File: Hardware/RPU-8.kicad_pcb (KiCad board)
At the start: 4 copper layers, 139.7 x 55.9 mm, 5 parts, among them J1 ADDR_BUS, J2 DATA_BUS, J3 Conn_01x03_Female, J4 CTRL_BUS, J5 INST_REG

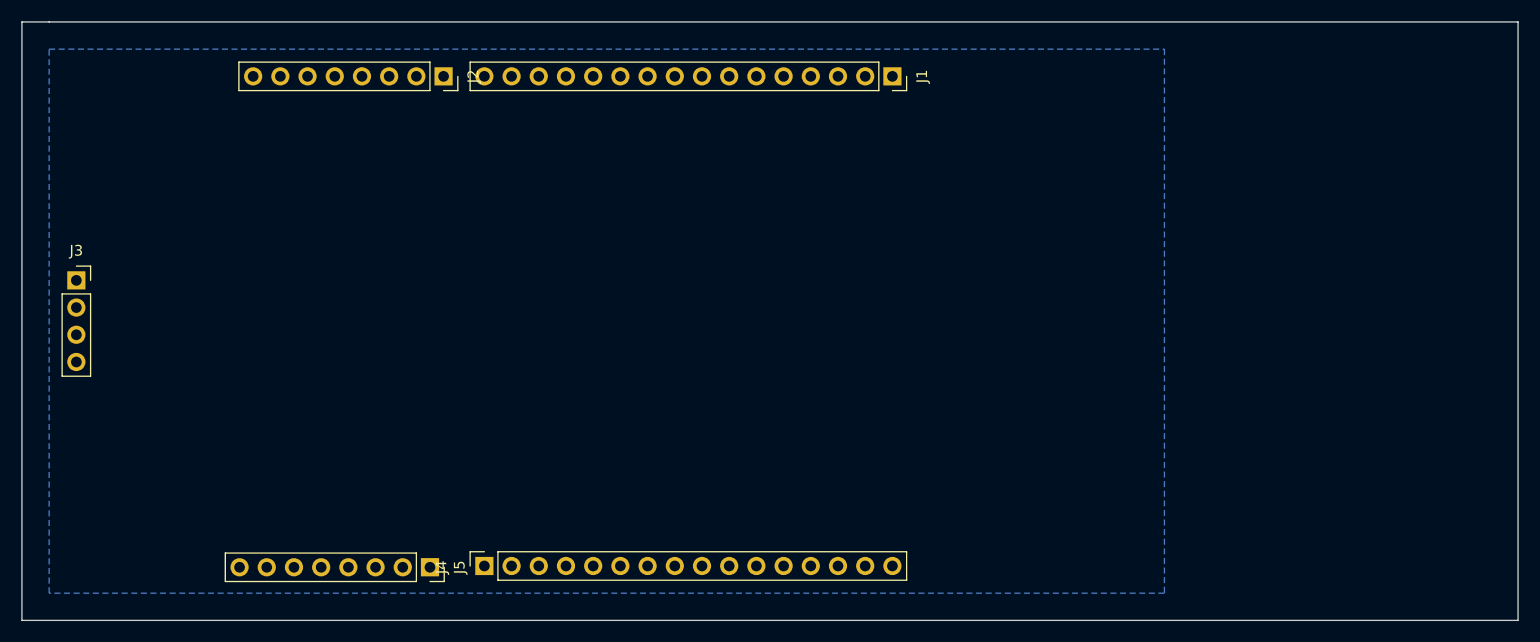
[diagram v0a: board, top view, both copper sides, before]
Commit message: fixed REG layout
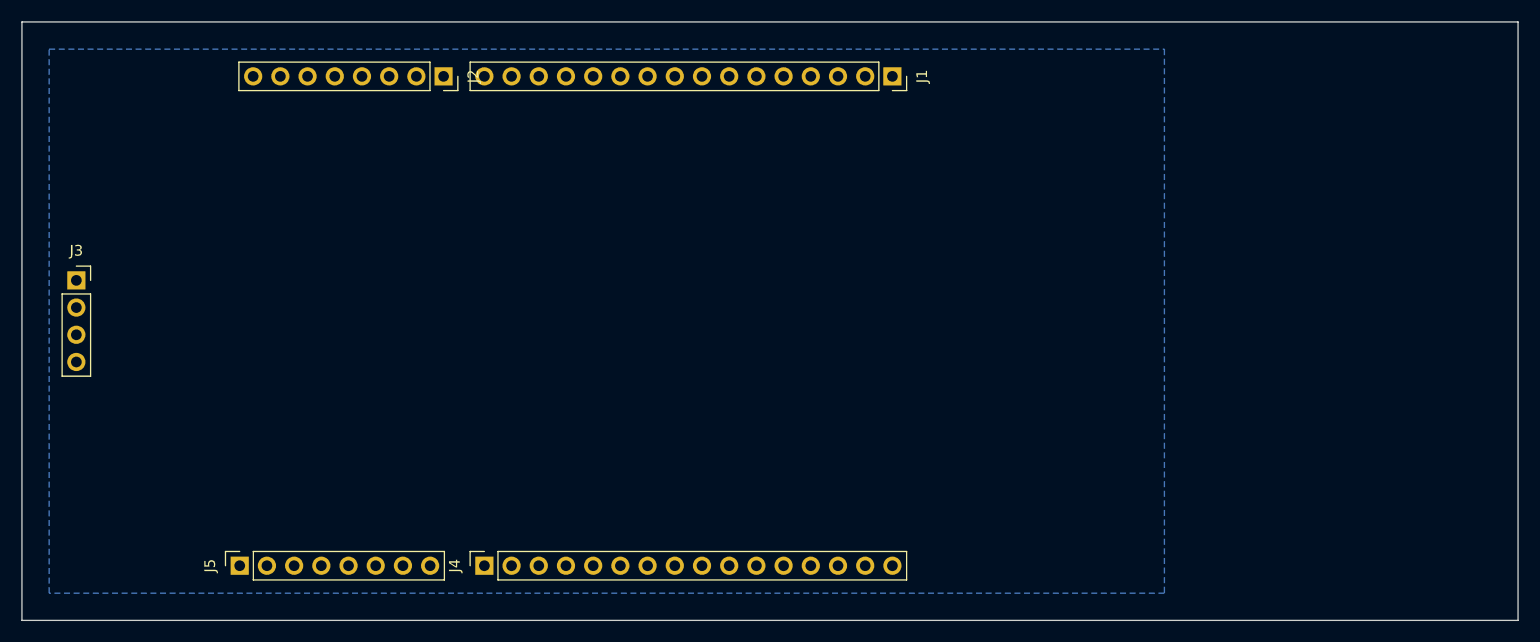
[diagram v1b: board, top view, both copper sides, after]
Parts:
- moved J5 17.8 mm to (82.6, 99.0), turned to 90 degrees
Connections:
- net A0 renamed /A0
- net A1 renamed /A1
- net A10 renamed /A10
- net A11 renamed /A11
- net A12 renamed /A12
- net A13 renamed /A13
- net A14 renamed /A14
- net A15 renamed /A15
- net A2 renamed /A2
- net A3 renamed /A3
- net A4 renamed /A4
- net A5 renamed /A5
- net A6 renamed /A6
- net A7 renamed /A7
- net A8 renamed /A8
- net A9 renamed /A9
- net C renamed /CLR
- net CE renamed /CE
- net CLK renamed /CLK
- net D0 renamed /D0
- net H renamed /HLT
- net Im renamed /Im
- net MI renamed /MI
- net MW renamed /MW
- net RI renamed /RI
- net RO renamed /RO
- net X renamed /X
- net ~{CI} renamed /~{CI}
- net ~{CO} renamed /~{CO}
- net ~{II} renamed /~{II}
- net ~{MO} renamed /~{MO}
- net ~{ΣI} renamed /~{ΣI}
- net ~{ΣO} renamed /ΣO
- J2 pad 2: (no net) -> /D1
- J2 pad 3: (no net) -> /D2
- J2 pad 4: (no net) -> /D3
- J2 pad 5: (no net) -> /D4
- J2 pad 6: (no net) -> /D5
- J2 pad 7: (no net) -> /D6
- J2 pad 8: (no net) -> /D7
- J3 pad 2: (no net) -> /RST
- J4 pad 2: (no net) -> /OI
- J5 pad 1: (no net) -> /I7
- J5 pad 2: (no net) -> /I6
- J5 pad 3: (no net) -> /I5
- J5 pad 4: (no net) -> /I4
- J5 pad 5: (no net) -> /I3
- J5 pad 6: (no net) -> /I2
- J5 pad 7: (no net) -> /I1
- J5 pad 8: (no net) -> /I0
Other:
- outline, holes or cut-outs redrawn
